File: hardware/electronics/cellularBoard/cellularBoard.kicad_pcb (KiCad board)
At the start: 4 copper layers, 22 x 36.8 mm, 58 parts, among them J1 M.2_E_Key_PCB_Edge, J2 Standoff, J3 0786463001, U1 LM51571-Q1, U2 SARA-R520-02B

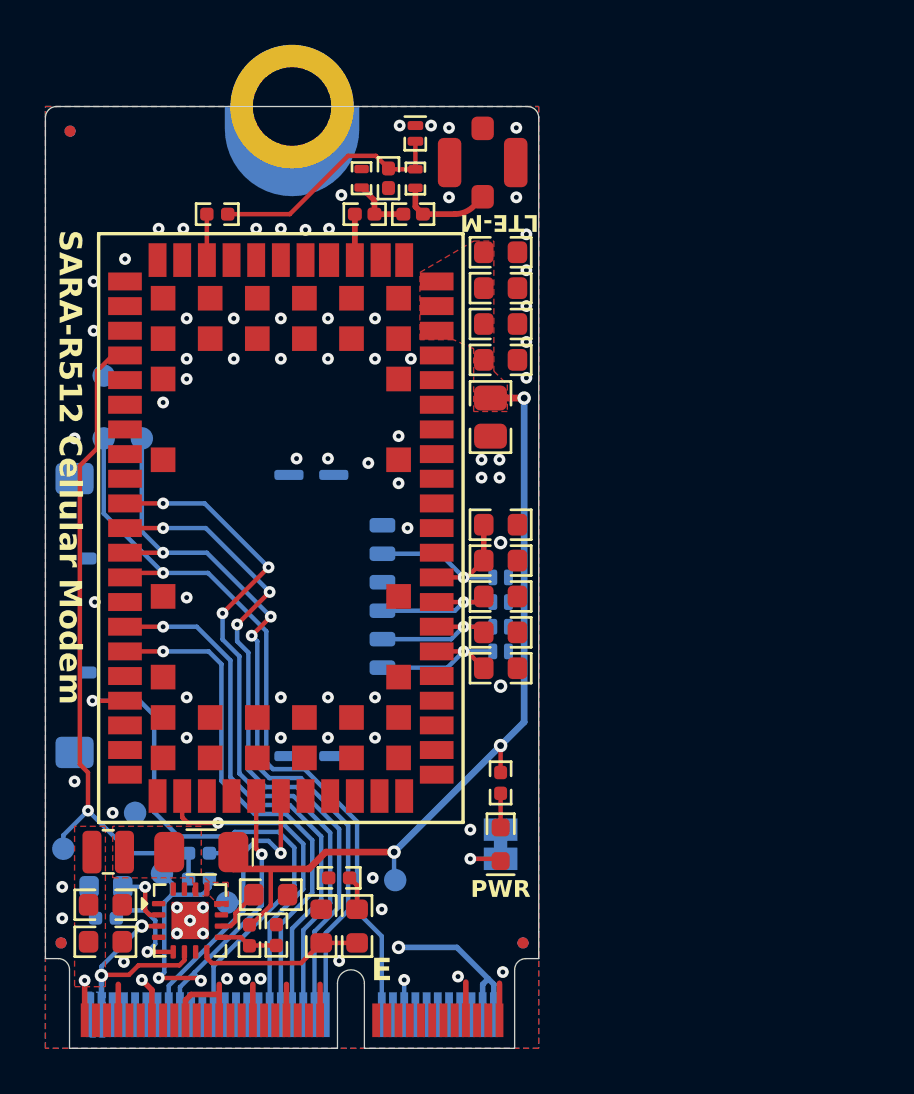
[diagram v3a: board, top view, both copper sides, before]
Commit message: moved components for fiducials
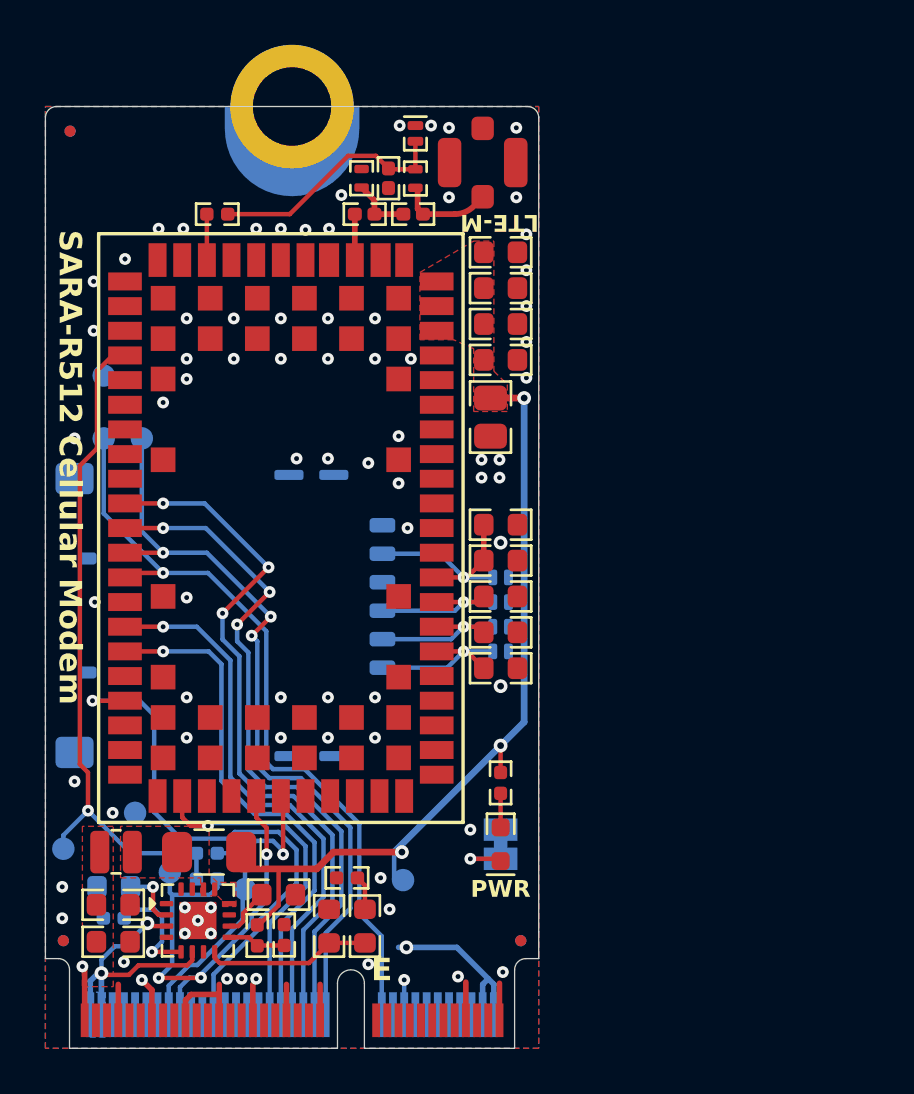
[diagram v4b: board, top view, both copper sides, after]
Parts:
- moved TP3 1.00 mm to (137.9, 112.9)
- moved TP4 0.35 mm to (134.6, 112.2)
- moved C8 0.35 mm to (132.1, 112.8)
- moved D1 0.35 mm to (136.3, 111.2)
- moved R6 0.35 mm to (132.1, 114.2)
- moved U1 0.35 mm to (135.8, 114.3)
- moved C1 0.35 mm to (132.0, 115.2)
- moved C10 0.35 mm to (141.7, 114.5)
- moved C11 0.35 mm to (143.2, 114.5)
- moved C2 0.35 mm to (132.0, 113.6)
- moved C9 0.35 mm to (139.4, 113.2)
- moved L1 0.35 mm to (132.2, 111.2)
- moved R1 0.35 mm to (138.4, 115.0)
- moved R3 0.35 mm to (136.2, 112.5)
- moved R4 0.35 mm to (136.2, 111.3)
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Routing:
- net +3V3: track 29.6 -> 32.9 mm
- net VSS: track 19.2 -> 19.8 mm
- net /SARA_SCL_1V8: track 15.5 -> 15.0 mm
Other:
- rule pad_to_mask_clearance: 0 -> 0.07
- board text added: "Madison Gleydura Master's Thesis 2025-01-01"
- board text removed: "Madison Gleydura Master's Thesis 2024-12-21"

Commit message: moved around vreg caps to center around notch
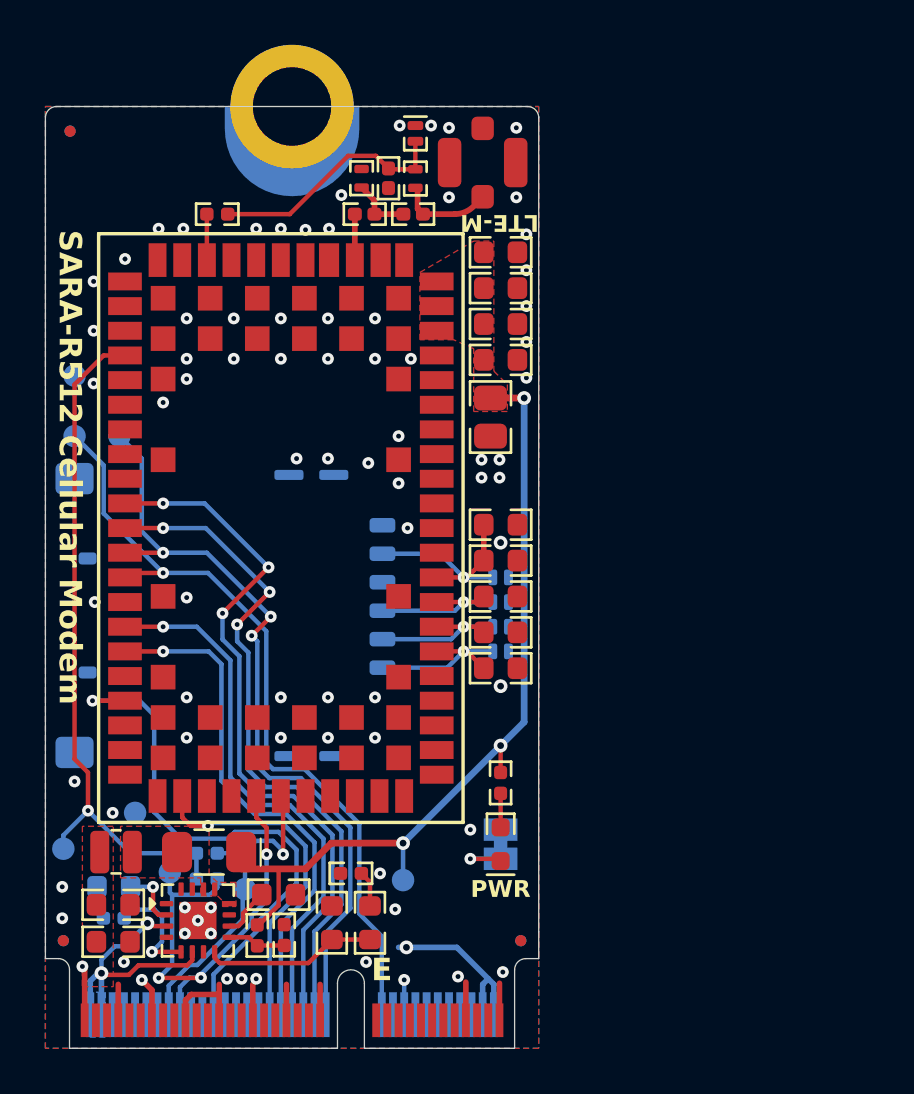
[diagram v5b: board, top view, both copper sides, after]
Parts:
- moved TP5 1.30 mm to (130.3, 92.7)
- moved TP8 1.30 mm to (130.3, 90.0)
- moved TP6 1.00 mm to (132.3, 92.7)
- moved C11 0.27 mm to (143.5, 114.4)
- moved R7 0.27 mm to (142.6, 112.2)
- moved C10 0.20 mm to (141.8, 114.4)
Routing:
- net /SARA_RXD_1V8: track 34.6 -> 35.3 mm
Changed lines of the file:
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@@
 	(footprint "lib_fp:MLCC0603"
 		(layer "F.Cu")
-		(at 143.25 114.55 90)
+		(at 143.475 114.4 90)
 		(descr "Capacitor, Chip; 1.60 mm L X 0.80 mm W X 0.88 mm H body")
 		(tags "0603; 1608")
@@
 	(footprint "lib_fp:MLCC0603"
 		(layer "F.Cu")
-		(at 141.65 114.55 90)
+		(at 141.775 114.4 90)
 		(descr "Capacitor, Chip; 1.60 mm L X 0.80 mm W X 0.88 mm H body")
 		(tags "0603; 1608")
@@
 	(footprint "lib_fp:CRCW0402"
 		(layer "F.Cu")
-		(at 142.45 112.4 180)
+		(at 142.625 112.2 180)
 		(descr "Resistor, Chip; 1.00 mm L X 0.50 mm W X 0.35 mm H body")
 		(tags "0402; 1005")
@@
 	(footprint "lib_fp:TP_1mm"
 		(layer "B.Cu")
-		(at 131.6 92.8 180)
+		(at 130.3 92.7 180)
 		(property "Reference" "TP5"
 			(at 0 2 0)
@@
 	(footprint "lib_fp:TP_1mm"
 		(layer "B.Cu")
-		(at 131.6 90 180)
+		(at 130.3 90 180)
 		(property "Reference" "TP8"
 			(at 0 2 0)
@@
 	(footprint "lib_fp:TP_1mm"
 		(layer "B.Cu")
-		(at 133.3 92.8 180)
+		(at 132.3 92.7 180)
 		(property "Reference" "TP6"
 			(at 0 2 0)
@@
 		)
 		(property "Value" "TXD"
-			(at -1.3 -0.9 0)
+			(at 0 1.1 0)
 			(unlocked yes)
 			(layer "B.SilkS")
@@
 	)
 	(via
-		(at 143.4 116.25)
+		(at 143.3 116.15)
 		(size 0.5275)
 		(drill 0.215)
@@
 	)
 	(via
-		(at 130.3 92.8)
-		(size 0.5275)
-		(drill 0.215)
-		(layers "F.Cu" "B.Cu")
-		(net 1)
-	)
-	(via
 		(at 135.3 87.45)
 		(size 0.5275)
@@
 	)
 	(via
-		(at 144.35 113.8)
+		(at 144.6 113.8)
 		(size 0.5275)
 		(drill 0.215)
@@
 	)
 	(via
+		(at 143.925 112.2)
+		(size 0.5275)
+		(drill 0.215)
+		(layers "F.Cu" "B.Cu")
+		(free yes)
+		(net 1)
+	)
+	(via
 		(at 141.6 93.7)
 		(size 0.5275)
@@
 	)
 	(via
-		(at 143.95 112.4)
+		(at 141.6 87.45)
 		(size 0.5275)
 		(drill 0.215)
@@
 	)
 	(via
-		(at 141.6 87.45)
+		(at 137.4 89.25)
 		(size 0.5275)
 		(drill 0.215)
 		(layers "F.Cu" "B.Cu")
-		(free yes)
 		(net 1)
 	)
 	(via
-		(at 137.4 89.25)
+		(at 131.15 90.35)
 		(size 0.5275)
 		(drill 0.215)
 		(layers "F.Cu" "B.Cu")
+		(free yes)
 		(net 1)
 	)
@@
 	)
 	(segment
-		(start 130.53625 94.01375)
-		(end 131.3 93.25)
+		(start 130.3 107.1)
+		(end 130.3 90.4)
 		(width 0.2)
 		(layer "F.Cu")
@@
 	(segment
 		(start 130.9 107.7)
-		(end 130.53625 107.33625)
+		(end 130.3 107.1)
 		(width 0.2)
 		(layer "F.Cu")
@@
 	)
 	(segment
-		(start 131.3 89.8)
-		(end 131.99874 89.10126)
+		(start 130.3 90.4)
+		(end 131.59874 89.10126)
 		(width 0.2)
 		(layer "F.Cu")
@@
 	)
 	(segment
-		(start 131.99874 89.10126)
+		(start 131.59874 89.10126)
 		(end 132.54929 89.10126)
 		(width 0.2)
@@
 		(net 4)
 	)
-	(segment
-		(start 131.3 93.25)
-		(end 131.3 89.8)
-		(width 0.2)
-		(layer "F.Cu")
-		(net 4)
-	)
-	(segment
-		(start 130.53625 107.33625)
-		(end 130.53625 94.01375)
-		(width 0.2)
-		(layer "F.Cu")
-		(net 4)
-	)
 	(via
 		(at 130.9 109.4)
@@
 	)
 	(segment
-		(start 141.65 115.3)
-		(end 143.25 115.3)
+		(start 141.775 115.15)
+		(end 143.475 115.15)
 		(width 0.2)
 		(layer "F.Cu")
@@
 	)
 	(segment
-		(start 136.55 115.975)
-		(end 136.775 116.2)
+		(start 140.725 116.2)
+		(end 141.775 115.15)
 		(width 0.2)
 		(layer "F.Cu")
@@
 	)
 	(segment
-		(start 140.75 116.2)
-		(end 141.65 115.3)
+		(start 136.775 116.2)
+		(end 140.725 116.2)
 		(width 0.2)
 		(layer "F.Cu")
@@
 	)
 	(segment
-		(start 136.775 116.2)
-		(end 140.75 116.2)
+		(start 136.55 115.975)
+		(end 136.775 116.2)
 		(width 0.2)
 		(layer "F.Cu")
@@
 	)
 	(segment
-		(start 137.73 111.25)
-		(end 137.73 112)
-		(width 0.3)
-		(layer "F.Cu")
-		(net 7)
-	)
-	(segment
-		(start 141.1 112)
-		(end 141.85 111.25)
+		(start 141.75 110.85)
+		(end 140.6 112)
 		(width 0.3)
 		(layer "F.Cu")
@@
 	)
 	(segment
-		(start 141.85 111.25)
-		(end 144.9 111.25)
-		(width 0.3)
+		(start 138.523242 114.5)
+		(end 138.45 114.5)
+		(width 0.2)
 		(layer "F.Cu")
 		(net 7)
 	)
 	(segment
-		(start 138.523242 114.5)
-		(end 138.45 114.5)
-		(width 0.2)
+		(start 137.73 112)
+		(end 137.73 111.25)
+		(width 0.3)
 		(layer "F.Cu")
 		(net 7)
@@
 	)
 	(segment
-		(start 137.73 112)
-		(end 141.1 112)
+		(start 144.95 110.85)
+		(end 141.75 110.85)
 		(width 0.3)
 		(layer "F.Cu")
@@
 		(net 7)
 	)
+	(segment
+		(start 140.6 112)
+		(end 137.73 112)
+		(width 0.3)
+		(layer "F.Cu")
+		(net 7)
+	)
 	(via
 		(at 149.3 106.5)
@@
 	)
 	(via
-		(at 144.9 111.25)
+		(at 144.95 110.85)
 		(size 0.615)
 		(drill 0.3)
@@
 	)
 	(segment
-		(start 144.55 111.25)
-		(end 149.3 106.5)
-		(width 0.3)
-		(layer "B.Cu")
-		(net 7)
-	)
-	(segment
-		(start 144.55 112.45)
-		(end 144.6 112.5)
+		(start 144.95 110.85)
+		(end 144.95 112.5)
 		(width 0.2)
 		(layer "B.Cu")
@@
 	)
 	(segment
-		(start 144.55 111.25)
-		(end 144.55 112.45)
-		(width 0.2)
+		(start 144.95 110.85)
+		(end 149.3 106.5)
+		(width 0.3)
 		(layer "B.Cu")
 		(net 7)
@@
 	)
 	(segment
-		(start 143.25 112.735)
-		(end 142.915 112.4)
+		(start 143.475 112.585)
+		(end 143.09 112.2)
 		(width 0.2)
 		(layer "F.Cu")
@@
 	)
 	(segment
-		(start 143.25 113.8)
-		(end 143.25 112.735)
+		(start 143.475 113.65)
+		(end 143.475 112.585)
 		(width 0.2)
 		(layer "F.Cu")
@@
 	)
 	(segment
-		(start 131.6 92.8)
-		(end 131.6 96.15)
+		(start 144 115)
+		(end 143 114)
 		(width 0.2)
 		(layer "B.Cu")
@@
 	)
 	(segment
-		(start 144 115)
-		(end 143 114)
+		(start 130.3 92.7)
+		(end 131.6 94)
 		(width 0.2)
 		(layer "B.Cu")
@@
 	)
 	(segment
-		(start 131.6 96.15)
-		(end 134.25 98.8)
+		(start 139.15176 107.55)
+		(end 138.85 107.24824)
 		(width 0.2)
 		(layer "B.Cu")
@@
 	)
 	(segment
-		(start 139.15176 107.55)
-		(end 138.85 107.24824)
+		(start 131.6 96.15)
+		(end 134.25 98.8)
 		(width 0.2)
 		(layer "B.Cu")
@@
 	)
 	(segment
+		(start 131.6 94)
+		(end 131.6 96.15)
+		(width 0.2)
+		(layer "B.Cu")
+		(net 39)
+	)
+	(segment
 		(start 138.85 101.4)
 		(end 136.25 98.8)
@@
 	(segment
 		(start 133.3 96.95)
-		(end 133.3 92.5)
+		(end 133.3 93.7)
 		(width 0.2)
 		(layer "B.Cu")
@@
 		(width 0.2)
 		(layer "B.Cu")
+		(net 42)
+	)
+	(segment
+		(start 133.3 93.7)
+		(end 132.3 92.7)
+		(width 0.2)
+		(layer "B.Cu")
